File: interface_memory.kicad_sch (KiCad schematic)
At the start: 3 parts, among them IC509 M41464, IC510 M41464, IC512 LC3517BML

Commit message: Add proper scans, redo traces.
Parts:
- added IC513, IC514: ~, Package_SO:SSOP-32_11.305x20.495mm_P1.27mm, symbol PC-Engine:D43100AGW
- added IC515: ~, Package_SO:SSOP-32_11.305x20.495mm_P1.27mm, symbol PC-Engine:D23HC4001EGW
- added IC516, IC517, IC518: 74LS244, Package_SO:SO-20_5.3x12.6mm_P1.27mm, symbol 74xx:74LS244
- added IC519: 74F32, Package_SO:SO-14_5.3x10.2mm_P1.27mm, symbol 74xx:74LS32
- added IC520: 74LS245, Package_SO:SO-20_5.3x12.6mm_P1.27mm, symbol 74xx:74LS245
- added R105 (x2): N/P, Resistor_SMD:R_0805_2012Metric, symbol Device:R
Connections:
- net XA7: now reaches IC512.1 (A7)
- net XA7: now also IC513.5 (A7), IC514.5 (A7), IC515.5 (A7), IC516.9 (O0b)
- net XD1: now reaches IC512.10 (IO2)
- net XD1: now also IC513.14 (I/O2), IC514.14 (I/O2), IC515.14 (Q1), IC520.12 (B6)
- net XD2: now reaches IC512.11 (IO3)
- net XD2: now also IC513.15 (I/O3), IC514.15 (I/O3), IC515.15 (Q2), IC520.13 (B5)
- net XD3: now reaches IC512.13 (IO4)
- net XD3: now also IC513.17 (I/O4), IC514.17 (I/O4), IC515.17 (Q3), IC520.14 (B4)
- net XD4: now reaches IC512.14 (IO5)
- net XD4: now also IC513.18 (I/O5), IC514.18 (I/O5), IC515.18 (Q4), IC520.15 (B3)
- net XD5: now reaches IC512.15 (IO6)
- net XD5: now also IC513.19 (I/O6), IC514.19 (I/O6), IC515.19 (Q5), IC520.16 (B2)
- net XD6: now reaches IC512.16 (IO7)
- net XD6: now also IC513.20 (I/O7), IC514.20 (I/O7), IC515.20 (Q6), IC520.17 (B1)
- net XD7: now reaches IC512.17 (IO8)
- net XD7: now also IC513.21 (I/O8), IC514.21 (I/O8), IC515.21 (Q7), IC520.18 (B0)
- net ~{XBRAM}: now reaches IC512.18 (~{CE})
- net XA10: now reaches IC512.19 (A10)
- net XA10: now also IC513.23 (A10), IC514.23 (A10), IC515.23 (A10), IC517.7 (O1b)
- net XA6: now reaches IC512.2 (A6)
- net XA6: now also IC513.6 (A6), IC514.6 (A6), IC515.6 (A6), IC516.12 (O3a)
- net ~{XOE}: now reaches IC512.20 (~{OE})
- net ~{XOE}: now also IC513.24 (OE), IC514.24 (OE), IC519.6, R105.1, R105.2
- net ~{XWE}: now reaches IC512.21 (~{WE})
- net ~{XWE}: now also IC513.29 (WE), IC514.29 (WE), IC519.3, R105.1, R105.2
- net XA9: now reaches IC512.22 (A9)
- net XA9: now also IC513.26 (A9), IC514.26 (A9), IC515.26 (A9), IC517.5 (O2b)
- net XA8: now reaches IC512.23 (A8)
- net XA8: now also IC513.27 (A8), IC514.27 (A8), IC515.27 (A8), IC517.16 (O1a)
- net XA5: now reaches IC512.3 (A5)
- net XA5: now also IC513.7 (A5), IC514.7 (A5), IC515.7 (A5), IC516.7 (O1b)
- net XA4: now reaches IC512.4 (A4)
- net XA4: now also IC513.8 (A4), IC514.8 (A4), IC515.8 (A4), IC516.14 (O2a)
- net XA3: now reaches IC512.5 (A3)
- net XA3: now also IC513.9 (A3), IC514.9 (A3), IC515.9 (A3), IC516.5 (O2b)
- net XA2: now reaches IC512.6 (A2)
- net XA2: now also IC513.10 (A2), IC514.10 (A2), IC515.10 (A2), IC516.16 (O1a)
- net XA1: now reaches IC512.7 (A1)
- net XA1: now also IC513.11 (A1), IC514.11 (A1), IC515.11 (A1), IC516.3 (O3b)
- net XA0: now reaches IC512.8 (A0)
- net XA0: now also IC513.12 (A0), IC514.12 (A0), IC515.12 (A0), IC516.18 (O0a)
- net XD0: now reaches IC512.9 (IO1)
- net XD0: now also IC513.13 (I/O1), IC514.13 (I/O1), IC515.13 (Q0), IC520.11 (B7)
- new net A0: IC516.2 (I0a)
- new net A1: IC516.17 (I3b)
- new net A10: IC517.13 (I1b)
- new net A11: IC517.6 (I2a)
- new net A12: IC517.8 (I3a)
- new net A13: IC517.17 (I3b)
- new net A14: IC517.2 (I0a)
- new net A15: IC517.11 (I0b)
- new net A16: IC518.2 (I0a)
- new net A17: IC518.4 (I1a)
- new net A18: IC518.6 (I2a)
- new net A2: IC516.4 (I1a)
- new net A3: IC516.15 (I2b)
- new net A4: IC516.6 (I2a)
- new net A5: IC516.13 (I1b)
- new net A6: IC516.8 (I3a)
- new net A7: IC516.11 (I0b)
- new net A8: IC517.4 (I1a)
- new net A9: IC517.15 (I2b)
- new net D0: IC520.9 (A7)
- new net D1: IC520.8 (A6)
- new net D2: IC520.7 (A5)
- new net D3: IC520.6 (A4)
- new net D4: IC520.5 (A3)
- new net D5: IC520.4 (A2)
- new net D6: IC520.3 (A1)
- new net D7: IC520.2 (A0)
- new net GND: IC518.1 (OEa), IC518.10 (GND), IC518.11 (I0b), IC518.13 (I1b), IC518.15 (I2b), IC518.17 (I3b), IC518.19 (OEb), IC519.10, IC519.12, IC519.13, IC519.2, IC519.5, IC519.7 (GND), IC519.9
- new net XA11: IC513.25 (A11), IC514.25 (A11), IC515.25 (A11), IC517.14 (O2a)
- new net XA12: IC513.4 (A12), IC514.4 (A12), IC515.4 (A12), IC517.12 (O3a)
- new net XA13: IC513.28 (A13), IC514.28 (A13), IC515.28 (A13), IC517.3 (O3b)
- new net XA14: IC513.3 (A14), IC514.3 (A14), IC515.29 (A14), IC517.18 (O0a)
- new net XA15: IC513.31 (A15), IC514.31 (A15), IC515.3 (A15), IC517.9 (O0b)
- new net XA16: IC513.2 (A16), IC514.2 (A16), IC515.2 (A16), IC518.18 (O0a)
- new net XA17: IC515.30 (A17), IC518.16 (O1a)
- new net XA18: IC515.31 (A18), IC518.14 (O2a)
- new net XDIR: IC520.1 (A->B)
- new net ~{RD}: IC515.24 (~{OE}), IC519.4
- new net ~{ROM}: IC515.22 (~{CE})
- new net ~{WR}: IC519.1
- new net ~{XCE}: IC520.19 (CE)
- new net ~{XRAM1}: IC513.22 (~{CE1})
- new net ~{XRAM2}: IC514.22 (~{CE1})
- no-connect marks 0 -> 6
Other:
- moved on the sheet: IC512

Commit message: More tracing.
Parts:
- added L106 (x2): ~, Inductor_SMD:L_0805_2012Metric, symbol Device:L
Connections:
- net GND: now also IC509.18 (VSS), IC510.18 (VSS), IC512.12 (VSS), IC513.16 (VSS), IC514.16 (VSS), IC515.16 (VSS), IC516.10 (GND), IC517.10 (GND), IC520.10 (GND)
- net ID0: now also IC509.2 (DQ1), IC510.2 (DQ1)
- net ID1: now also IC509.3 (DQ2), IC510.3 (DQ2)
- net ID2: now also IC509.15 (DQ3), IC510.15 (DQ3)
- net ID3: now also IC509.17 (DQ4), IC510.17 (DQ4)
- net +5V: now reaches IC516.20 (VCC)
- net +5V: now also IC509.9 (VCC), IC510.9 (VCC), IC512.24 (VCC), IC515.32 (VCC), IC517.20 (VCC), IC518.20 (VCC), IC520.20 (VCC), L106.1, L106.1
- net at IC514.30 (CE2): now also IC514.32 (VCC), L106.2
- net at IC513.30 (CE2): now also IC513.32 (VCC), L106.2
- net ~{IOE} renamed ~{IOE0}
- net ~{IOE0}: no longer IC510.1 (~{OE})
- net ~{IW} renamed ~{IW0}
- net ~{IW0}: no longer IC510.4 (~{W})
- new net ~{IOE1}: IC510.1 (~{OE})
- new net ~{IW1}: IC510.4 (~{W})

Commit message: Yet more tracing.
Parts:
- added L106 (x5): ~, Inductor_SMD:L_0805_2012Metric, symbol Device:L
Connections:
- net +5V: no longer IC512.24 (VCC), IC515.32 (VCC), IC516.20 (VCC), IC517.20 (VCC), IC518.20 (VCC), IC520.20 (VCC)
- net GND: now also IC516.1 (OEa), IC516.19 (OEb)
- net at IC519.14 (VCC): now also L106.2
- net at IC517.1 (OEa): now also IC517.19 (OEb)
- new net: IC517.20 (VCC), L106.2
- new net: IC516.20 (VCC), L106.2
- new net: IC520.20 (VCC), L106.2
- new net: IC518.20 (VCC), L106.2
- new net +5VD: L106.1, L106.1, L106.1, L106.1, L106.1

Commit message: IC routing mostly complete, start adding passives.
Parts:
- L106: footprint Inductor_SMD:L_0805_2012Metric -> A-PCENGINE:SMD_0805_Narrow
- R105: footprint Resistor_SMD:R_0805_2012Metric -> A-PCENGINE:SMD_0805_Narrow
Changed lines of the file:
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@@
       (effects (font (size 1.27 1.27)))
     )
-    (property "Footprint" "Inductor_SMD:L_0805_2012Metric" (at 372.11 138.43 0)
+    (property "Footprint" "A-PCENGINE:SMD_0805_Narrow" (at 372.11 138.43 0)
       (effects (font (size 1.27 1.27)) hide)
     )
@@
       (effects (font (size 1.27 1.27)))
     )
-    (property "Footprint" "Resistor_SMD:R_0805_2012Metric" (at 96.52 209.042 90)
+    (property "Footprint" "A-PCENGINE:SMD_0805_Narrow" (at 96.52 209.042 90)
       (effects (font (size 1.27 1.27)) hide)
     )
@@
       (effects (font (size 1.27 1.27)))
     )
-    (property "Footprint" "Resistor_SMD:R_0805_2012Metric" (at 96.52 206.502 90)
+    (property "Footprint" "A-PCENGINE:SMD_0805_Narrow" (at 96.52 206.502 90)
       (effects (font (size 1.27 1.27)) hide)
     )
@@
       (effects (font (size 1.27 1.27)))
     )
-    (property "Footprint" "Inductor_SMD:L_0805_2012Metric" (at 227.965 26.67 0)
+    (property "Footprint" "A-PCENGINE:SMD_0805_Narrow" (at 227.965 26.67 0)
       (effects (font (size 1.27 1.27)) hide)
     )
@@
       (effects (font (size 1.27 1.27)))
     )
-    (property "Footprint" "Inductor_SMD:L_0805_2012Metric" (at 372.11 88.9 0)
+    (property "Footprint" "A-PCENGINE:SMD_0805_Narrow" (at 372.11 88.9 0)
       (effects (font (size 1.27 1.27)) hide)
     )
@@
       (effects (font (size 1.27 1.27)))
     )
-    (property "Footprint" "Inductor_SMD:L_0805_2012Metric" (at 195.58 233.045 0)
+    (property "Footprint" "A-PCENGINE:SMD_0805_Narrow" (at 195.58 233.045 0)
       (effects (font (size 1.27 1.27)) hide)
     )
@@
       (effects (font (size 1.27 1.27)))
     )
-    (property "Footprint" "Inductor_SMD:L_0805_2012Metric" (at 142.24 175.26 0)
+    (property "Footprint" "A-PCENGINE:SMD_0805_Narrow" (at 142.24 175.26 0)
       (effects (font (size 1.27 1.27)) hide)
     )
@@
       (effects (font (size 1.27 1.27)))
     )
-    (property "Footprint" "Inductor_SMD:L_0805_2012Metric" (at 356.87 45.085 0)
+    (property "Footprint" "A-PCENGINE:SMD_0805_Narrow" (at 356.87 45.085 0)
       (effects (font (size 1.27 1.27)) hide)
     )
@@
       (effects (font (size 1.27 1.27)))
     )
-    (property "Footprint" "Inductor_SMD:L_0805_2012Metric" (at 208.28 175.26 0)
-      (effects (font (size 1.27 1.27)) hide)
-    )
+    (property "Footprint" "A-PCENGINE:SMD_0805_Narrow" (at 208.28 175.26 0)
+      (effects (font (size 1.27 1.27)) hide)
+    )

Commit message: More passives, custom footprints, etc.
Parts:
- added C105 (x7): ?, A-PCENGINE:CP_6x1.5mm, symbol Device:C_Polarized
- added C105 (x7): ?, A-PCENGINE:SMD_0805_Narrow, symbol Device:C
- IC512: footprint Package_SO:SOIC-24W_7.5x15.4mm_P1.27mm -> A-PCENGINE:SOIC-24W_P1.27mm
- IC513, IC514, IC515: footprint Package_SO:SSOP-32_11.305x20.495mm_P1.27mm -> A-PCENGINE:SSOP-32_P1.27mm
- IC516, IC517, IC518, IC520: footprint Package_SO:SO-20_5.3x12.6mm_P1.27mm -> A-PCENGINE:SO-20_P1.27mm_Gutters
- IC519: footprint Package_SO:SO-14_5.3x10.2mm_P1.27mm -> A-PCENGINE:SO-14_P1.27mm_Gutters
- L106: footprint A-PCENGINE:SMD_0805_Narrow -> A-PCENGINE:SMD_0805_Narrow_Long
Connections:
- net +5V: no longer L106.1, L106.1
- net +5VD: now also L106.1, L106.1
- net GND: now also IC517.1 (OEa), IC517.19 (OEb), C105.1, C105.1, C105.1, C105.1, C105.1, C105.1, C105.1, C105.2, C105.2, C105.2, C105.2, C105.2, C105.2, C105.2
- net at IC517.20 (VCC), L106.2: now also C105.1, C105.2
- net at IC516.20 (VCC), L106.2: now also C105.1, C105.2
- net at IC520.20 (VCC), L106.2: now also C105.1, C105.2
- net at IC518.20 (VCC), L106.2: now also C105.1, C105.2
- net at IC519.14 (VCC), L106.2: now also C105.1, C105.2
- net at IC514.30 (CE2), IC514.32 (VCC), L106.2: now also C105.1, C105.2
- net at IC513.30 (CE2), IC513.32 (VCC), L106.2: now also C105.1, C105.2
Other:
- moved on the sheet: L106

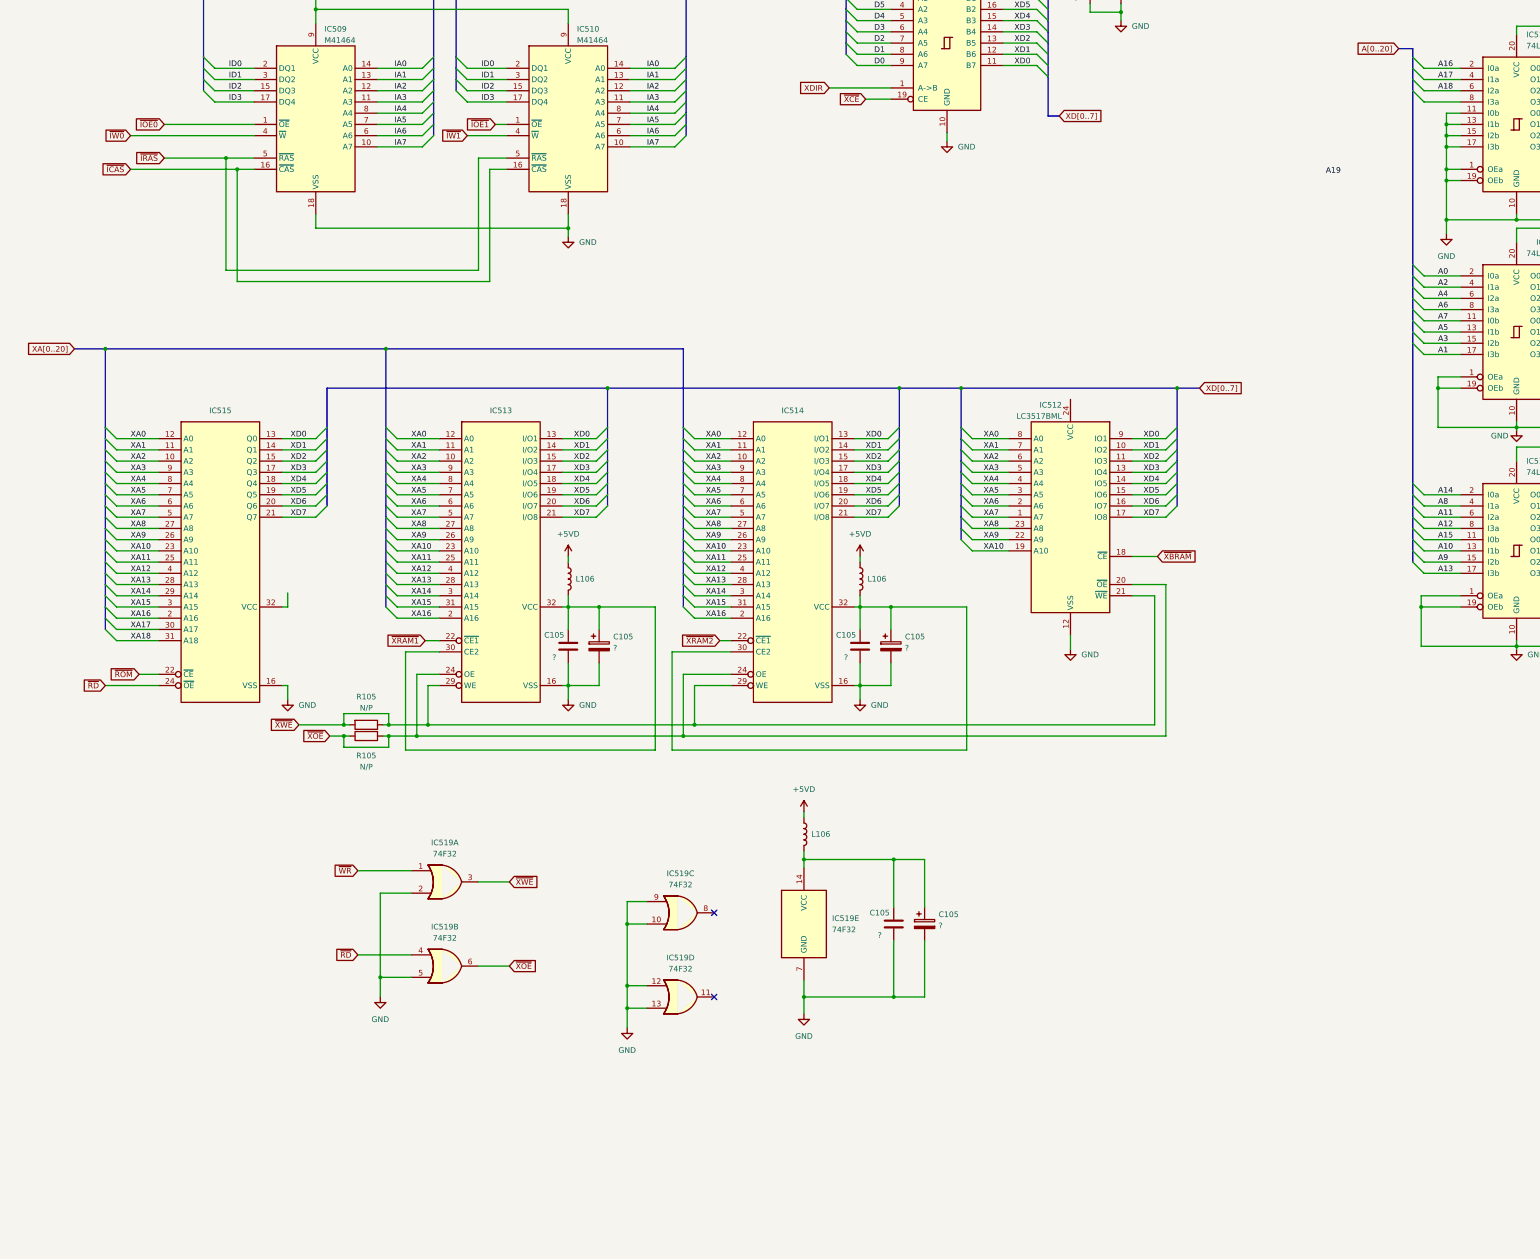
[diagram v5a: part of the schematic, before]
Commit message: Top layer first draft.
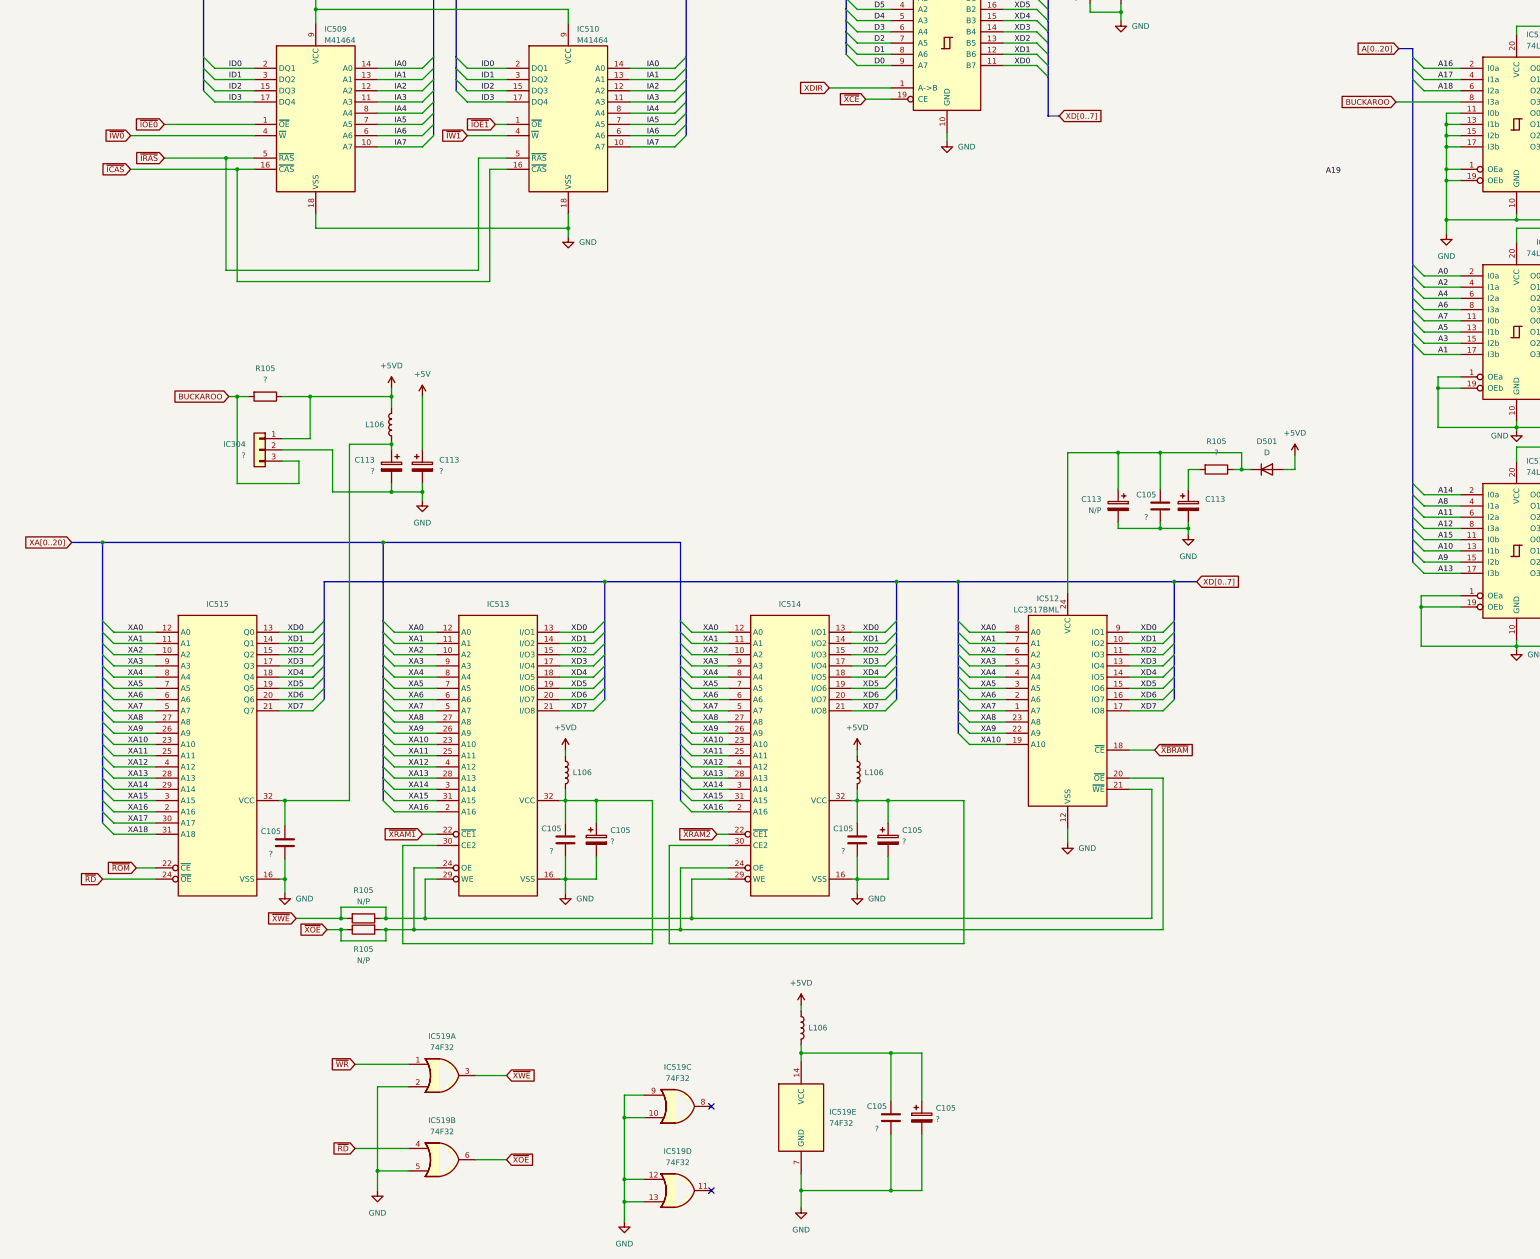
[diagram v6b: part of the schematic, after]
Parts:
- added C105 (x2): ?, A-PCENGINE:SMD_0805_Narrow, symbol Device:C
- added C113: N/P, A-PCENGINE:CP_6x1.5mm, symbol Device:C_Polarized
- added C113: ?, A-PCENGINE:CP_8x2mm, symbol Device:C_Polarized
- added C113: ~, A-PCENGINE:Elec_P5.00mm_D12mm_Pad3mm, symbol Device:C_Polarized
- added C113: ?, A-PCENGINE:CP_6x1.5mm, symbol Device:C_Polarized
- added D501: D, A-PCENGINE:Transistor_SMD, symbol Device:D
- added IC304: ?, A-PCENGINE:SOT-89-3, symbol Connector_Generic:Conn_01x03
- added L106: ~, A-PCENGINE:SMD_0805_Narrow, symbol Device:L
- added R105 (x2): ?, A-PCENGINE:SMD_0805_Narrow, symbol Device:R
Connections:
- net +5V: now also C113.1
- net +5VD: now also D501.2 (A), IC304.1 (Pin_1), L106.1, R105.1
- net GND: now also C105.1, C105.1, C113.2, C113.2, C113.2, C113.2, IC304.2 (Pin_2)
- net at IC512.24 (VCC): now also C105.2, C113.1, D501.1 (K), R105.1
- net BUCKAROO: now reaches IC518.8 (I3a)
- net BUCKAROO: now also IC304.3 (Pin_3), R105.2
- net at IC515.32 (VCC): now also C105.2, C113.1, L106.2
- new net: C113.1, R105.2
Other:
- moved on the sheet: C105, IC512, IC513, IC514, IC515, IC519A, IC519B, IC519C, IC519D, IC519E, L106, R105
